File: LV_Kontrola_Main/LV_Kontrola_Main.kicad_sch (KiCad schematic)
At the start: 0 parts

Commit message: Folder structure added
Added a folder structure for documentation, code and component data; Added basic info to KiCad files
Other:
- company: (none) -> "Black Hornets" Formula Student team
- title: (none) -> LV_Kontrola_Main
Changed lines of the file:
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@@
 	(generator_version "9.0")
 	(paper "A4")
+	(title_block
+		(title "LV_Kontrola_Main")
+		(rev "1.00A")
+		(company "\"Black Hornets\" Formula Student team")
+		(comment 1 "Authors: Dusan Novkovic; Nikola Popovic")
+		(comment 2 "Subteam: Low Voltage team")
+	)
 	(sheet_instances
 		(path "/"

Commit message: Added a lot
Created a schematic hierarchy for LV_Regulator, added connectors, added start logic, added address select jumpers for RS485, implemented start isolation on LV_Kontrola_Main,...
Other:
- added sheet Start_3V3_Isolation (Start_3V3_Isolation.kicad_sch)
- added sheet Start_5V_Isolation (Start_5V_Isolation.kicad_sch)
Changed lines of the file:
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@@
 		(comment 2 "Subteam: Low Voltage team")
+	)
+	(sheet
+		(at 20.32 58.42)
+		(size 48.26 30.48)
+		(exclude_from_sim no)
+		(in_bom yes)
+		(on_board yes)
+		(dnp no)
+		(fields_autoplaced yes)
+		(stroke
+			(width 0.1524)
+			(type solid)
+		)
+		(fill
+			(color 0 0 0 0.0000)
+		)
+		(property "Sheetname" "Start_3V3_Isolation"
+			(at 20.32 57.7084 0)
+			(effects
+				(font
+					(size 1.27 1.27)
+				)
+				(justify left bottom)
+			)
+		)
+		(property "Sheetfile" "Start_3V3_Isolation.kicad_sch"
+			(at 20.32 89.4846 0)
+			(effects
+				(font
+					(size 1.27 1.27)
+				)
+				(justify left top)
+			)
+		)
+		(property "Field2" ""
+			(at 20.32 58.42 0)
+			(effects
+				(font
+					(size 1.27 1.27)
+				)
+			)
+		)
+		(instances
+			(project "LV_Kontrola_Main"
+				(path "/b33d6979-93a0-4110-9c2c-0d6314502d31"
+					(page "3")
+				)
+			)
+		)
+	)
+	(sheet
+		(at 20.32 20.32)
+		(size 48.26 30.48)
+		(exclude_from_sim no)
+		(in_bom yes)
+		(on_board yes)
+		(dnp no)
+		(fields_autoplaced yes)
+		(stroke
+			(width 0.1524)
+			(type solid)
+		)
+		(fill
+			(color 0 0 0 0.0000)
+		)
+		(property "Sheetname" "Start_5V_Isolation"
+			(at 20.32 19.6084 0)
+			(effects
+				(font
+					(size 1.27 1.27)
+				)
+				(justify left bottom)
+			)
+		)
+		(property "Sheetfile" "Start_5V_Isolation.kicad_sch"
+			(at 20.32 51.3846 0)
+			(effects
+				(font
+					(size 1.27 1.27)
+				)
+				(justify left top)
+			)
+		)
+		(property "Field2" ""
+			(at 20.32 20.32 0)
+			(effects
+				(font
+					(size 1.27 1.27)
+				)
+			)
+		)
+		(instances
+			(project "LV_Kontrola_Main"
+				(path "/b33d6979-93a0-4110-9c2c-0d6314502d31"
+					(page "2")
+				)
+			)
+		)
 	)
 	(sheet_instances

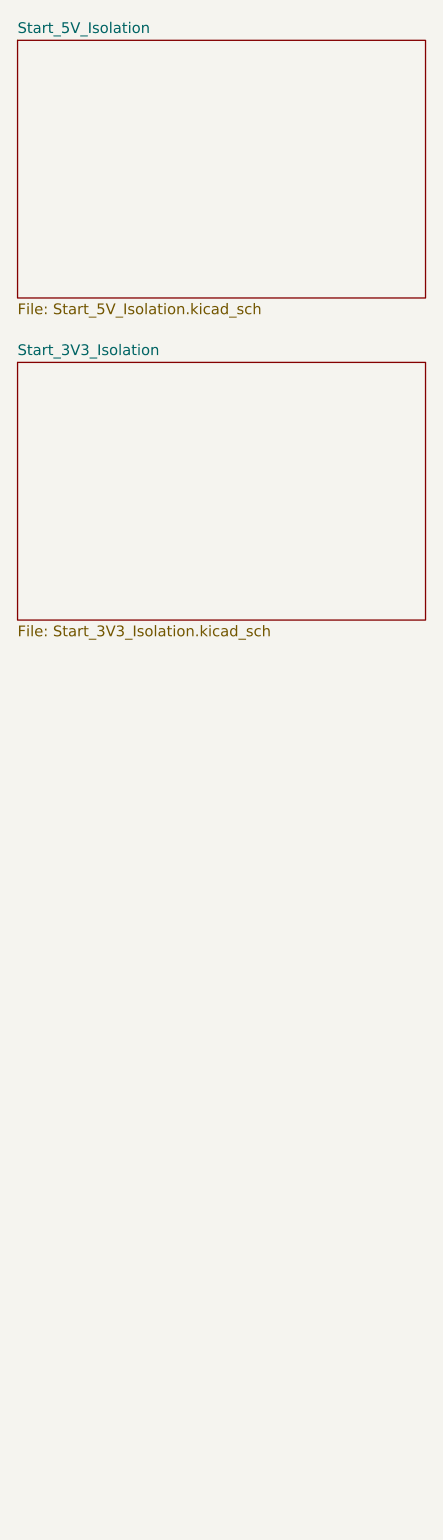
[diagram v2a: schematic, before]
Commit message: Added Start Control
Added Start Control MCU to the LV_Kontrola_Main, added hsc/lsc to LV_Regulator, fixed component numbering
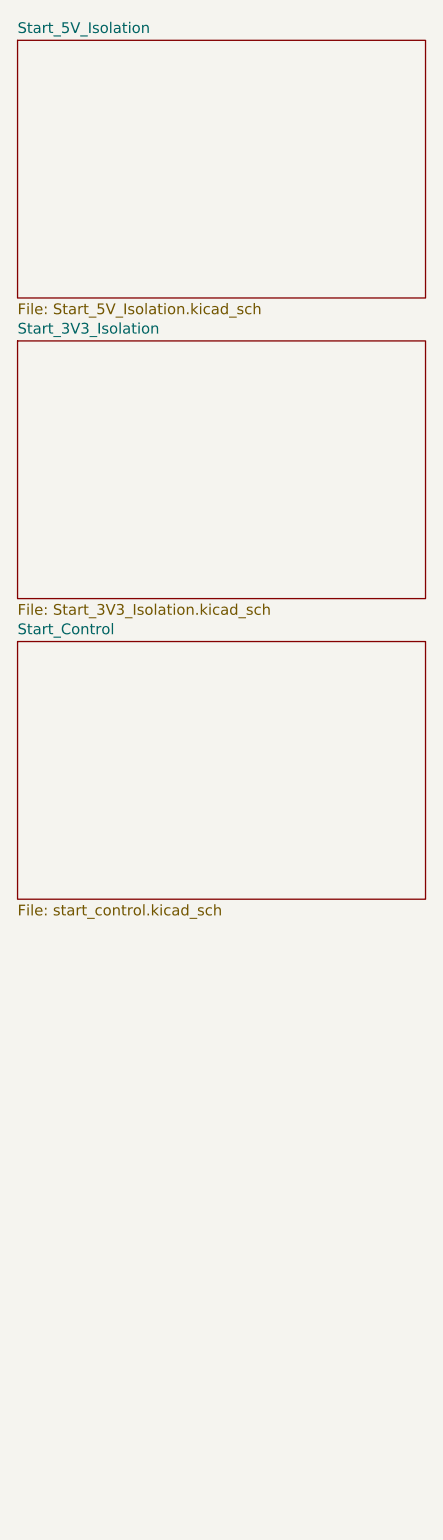
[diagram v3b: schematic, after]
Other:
- added sheet Start_Control (start_control.kicad_sch)
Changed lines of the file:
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@@
 	)
 	(sheet
-		(at 20.32 58.42)
+		(at 20.32 55.88)
 		(size 48.26 30.48)
 		(exclude_from_sim no)
@@
 		)
 		(property "Sheetname" "Start_3V3_Isolation"
-			(at 20.32 57.7084 0)
+			(at 20.32 55.1684 0)
 			(effects
 				(font
@@
 		)
 		(property "Sheetfile" "Start_3V3_Isolation.kicad_sch"
-			(at 20.32 89.4846 0)
+			(at 20.32 86.9446 0)
 			(effects
 				(font
@@
 		)
 		(property "Field2" ""
-			(at 20.32 58.42 0)
+			(at 20.32 55.88 0)
 			(effects
 				(font
@@
 				)
 			)
+		)
+	)
+	(sheet
+		(at 20.32 91.44)
+		(size 48.26 30.48)
+		(exclude_from_sim no)
+		(in_bom yes)
+		(on_board yes)
+		(dnp no)
+		(fields_autoplaced yes)
+		(stroke
+			(width 0.1524)
+			(type solid)
+		)
+		(fill
+			(color 0 0 0 0.0000)
+		)
+		(property "Sheetname" "Start_Control"
+			(at 20.32 90.7284 0)
+			(effects
+				(font
+					(size 1.27 1.27)
+				)
+				(justify left bottom)
+			)
+		)
+		(property "Sheetfile" "start_control.kicad_sch"
+			(at 20.32 122.5046 0)
+			(effects
+				(font
+					(size 1.27 1.27)
+				)
+				(justify left top)
+			)
+		)
+		(instances
+			(project "LV_Kontrola_Main"
+				(path "/b33d6979-93a0-4110-9c2c-0d6314502d31"
+					(page "4")
+				)
+			)

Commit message: Various changes
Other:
- added sheet Start_Power (Start_Power.kicad_sch)
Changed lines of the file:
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@@
+	)
+	(sheet
+		(at 20.32 127)
+		(size 48.26 30.48)
+		(exclude_from_sim no)
+		(in_bom yes)
+		(on_board yes)
+		(dnp no)
+		(fields_autoplaced yes)
+		(stroke
+			(width 0.1524)
+			(type solid)
+		)
+		(fill
+			(color 0 0 0 0.0000)
+		)
+		(property "Sheetname" "Start_Power"
+			(at 20.32 126.2884 0)
+			(effects
+				(font
+					(size 1.27 1.27)
+				)
+				(justify left bottom)
+			)
+		)
+		(property "Sheetfile" "Start_Power.kicad_sch"
+			(at 20.32 158.0646 0)
+			(effects
+				(font
+					(size 1.27 1.27)
+				)
+				(justify left top)
+			)
+		)
+		(instances
+			(project "LV_Kontrola_Main"
+				(path "/b33d6979-93a0-4110-9c2c-0d6314502d31"
+					(page "5")
+				)
+			)
+		)
 	)
 	(sheet

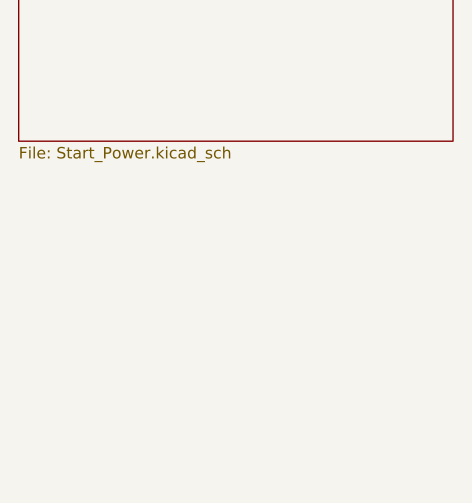
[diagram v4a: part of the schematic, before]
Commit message: Changes to LV_Kontrola_Main
Added a lot to the schematic, fixed component libs, mics...
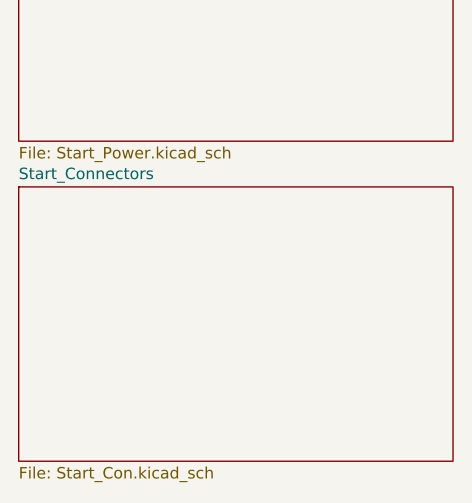
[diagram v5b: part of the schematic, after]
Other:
- added sheet Start_Connectors (Start_Con.kicad_sch)
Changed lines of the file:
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@@
+	)
+	(sheet
+		(at 20.32 162.56)
+		(size 48.26 30.48)
+		(exclude_from_sim no)
+		(in_bom yes)
+		(on_board yes)
+		(dnp no)
+		(fields_autoplaced yes)
+		(stroke
+			(width 0.1524)
+			(type solid)
+		)
+		(fill
+			(color 0 0 0 0.0000)
+		)
+		(property "Sheetname" "Start_Connectors"
+			(at 20.32 161.8484 0)
+			(effects
+				(font
+					(size 1.27 1.27)
+				)
+				(justify left bottom)
+			)
+		)
+		(property "Sheetfile" "Start_Con.kicad_sch"
+			(at 20.32 193.6246 0)
+			(effects
+				(font
+					(size 1.27 1.27)
+				)
+				(justify left top)
+			)
+		)
+		(instances
+			(project "LV_Kontrola_Main"
+				(path "/b33d6979-93a0-4110-9c2c-0d6314502d31"
+					(page "6")
+				)
+			)
+		)
 	)
 	(sheet
